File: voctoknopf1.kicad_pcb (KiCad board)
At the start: 2 copper layers, 161.2 x 88.5 mm, 47 parts, among them SW1 MX_D, SW10 MX_D, SW11 MX_D, SW12 MX_D, SW2 MX_D, SW3 MX_D, SW4 MX_D, SW5 MX_D, SW6 MX_D, SW7 MX_D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

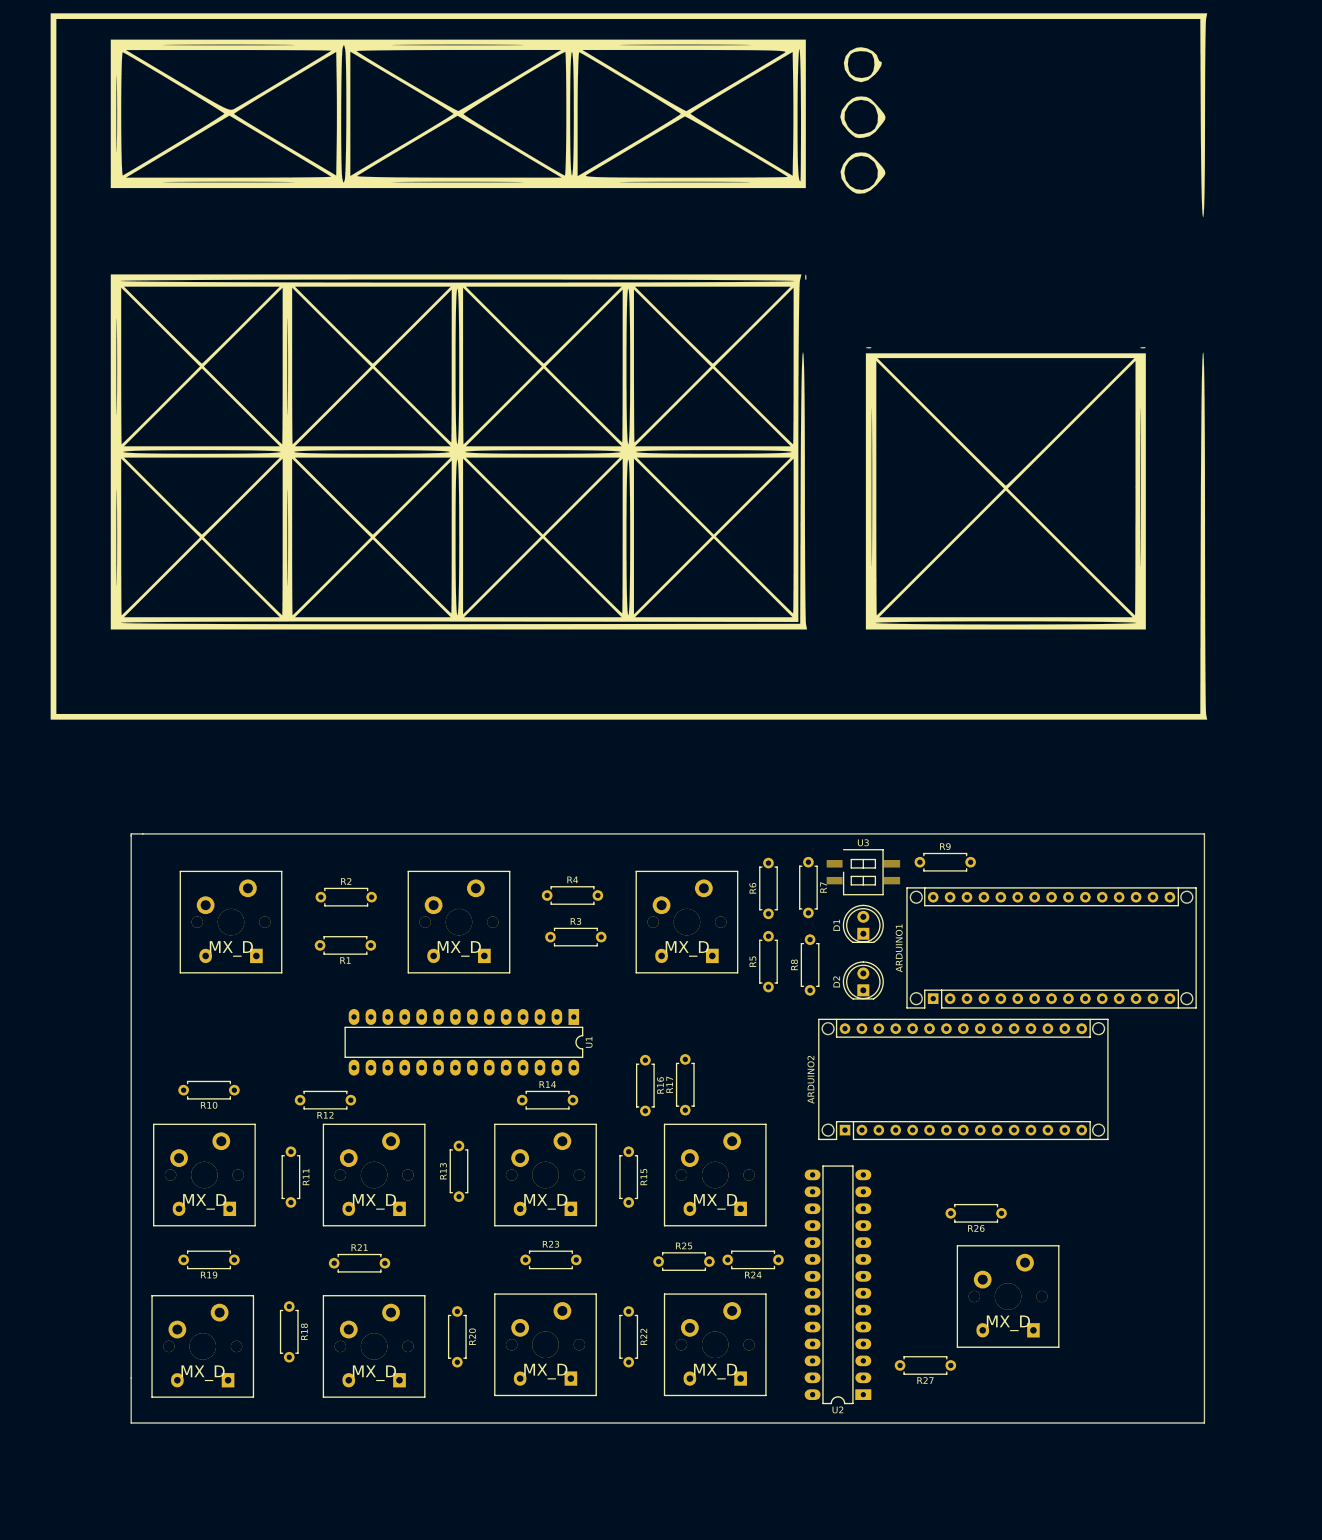
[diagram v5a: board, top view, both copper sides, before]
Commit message: ethernet shild the right way around
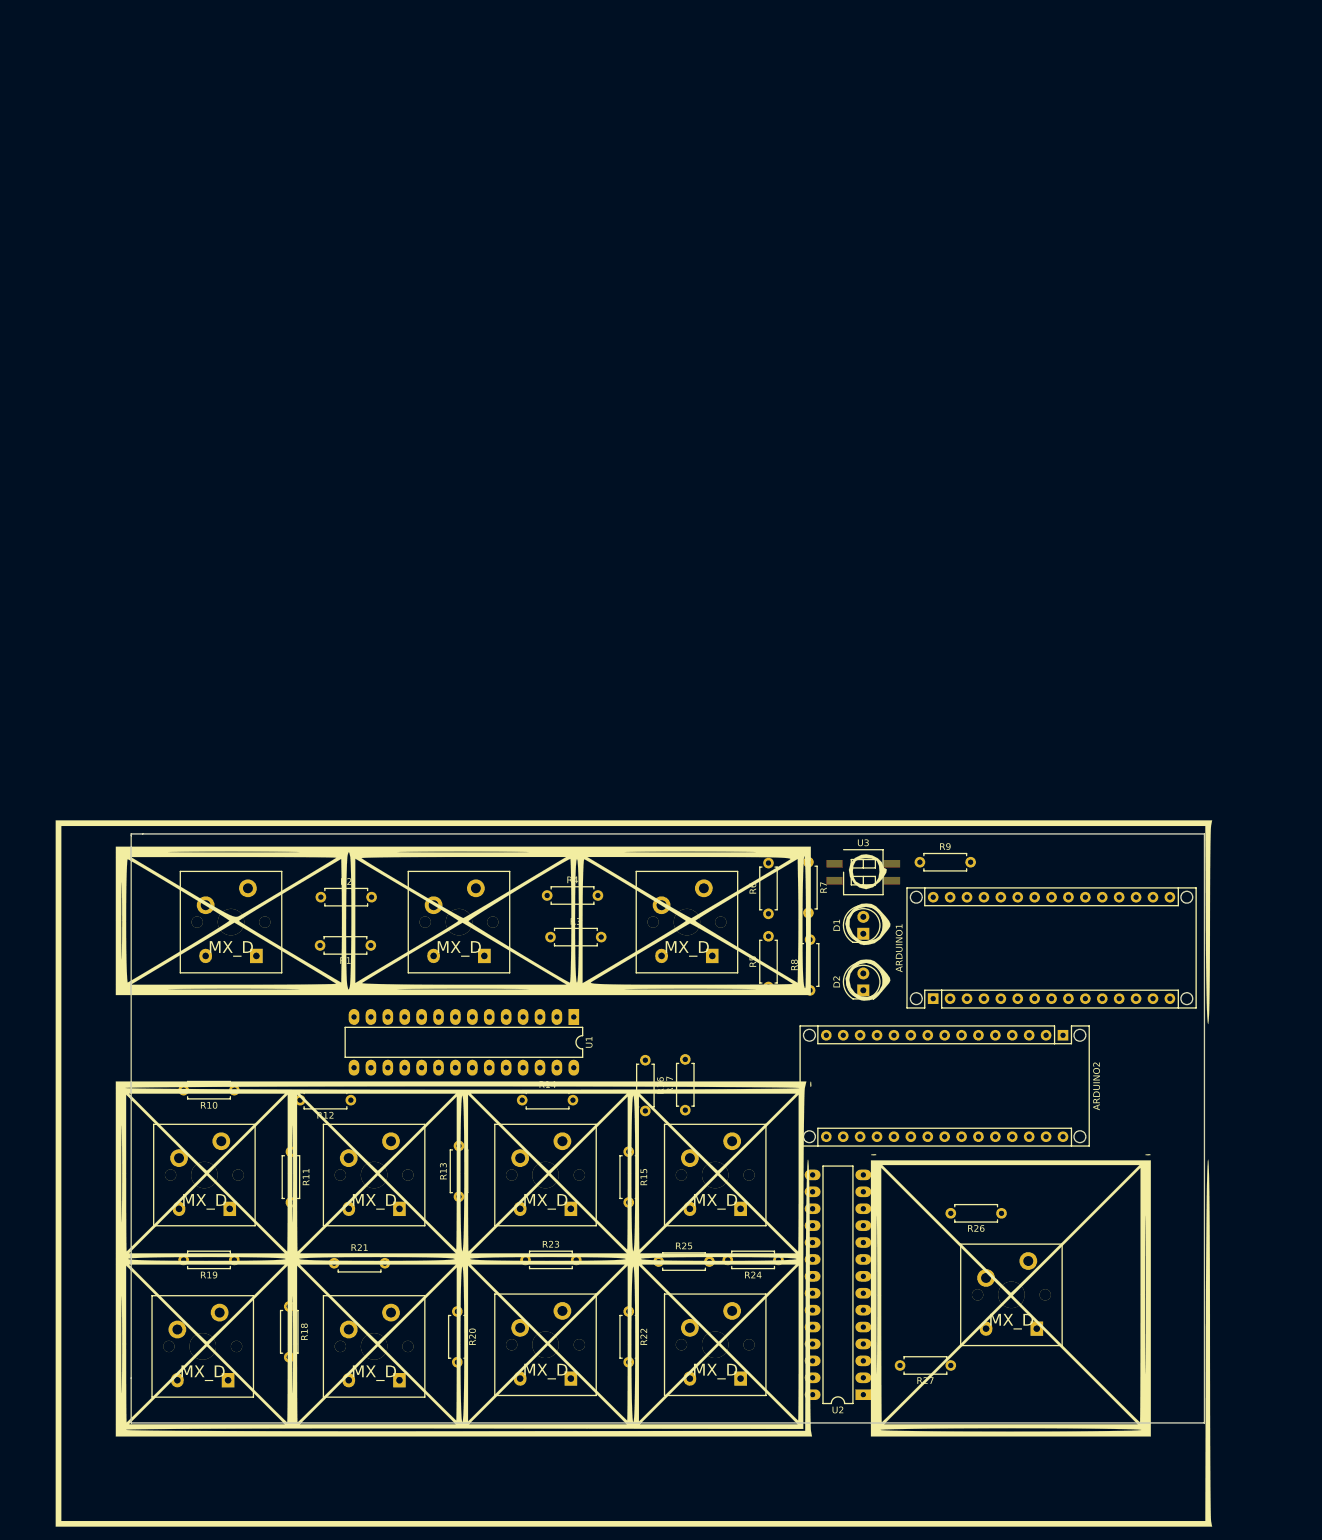
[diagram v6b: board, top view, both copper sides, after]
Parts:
- moved G*** 121.3 mm to (90.0, 66.5)
- moved ARDUINO2 35.7 mm to (156.2, 47.0), turned to 270 degrees
- moved SW12 0.56 mm to (148.5, 86.0)
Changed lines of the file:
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@@
     (links 118)
     (no_connects 118)
-    (area 16.174999 16.674999 177.575001 105.325001)
+    (area 4.654999 14.457221 179.185001 121.082778)
     (thickness 1.6)
     (drawings 7)
@@
   )
   (module cherry:SW_PCB_4PIN (layer F.Cu)
-    (at 148 86.25)
+    (at 148.5 86)
     (fp_text reference SW12 (at -4.445 -5.715) (layer F.SilkS) hide
       (effects (font (size 1.778 1.778) (thickness 0.2032)))
@@
   )
   (module Modules:Arduino_Nano_WithMountingHoles (layer F.Cu)
-    (at 123.5 61.25 90)
+    (at 156.25 47 270)
     (descr "Arduino Nano, http://www.mouser.com/pdfdocs/Gravitech_Arduino_Nano3_0.pdf")
     (tags "Arduino Nano")
-    (fp_text reference ARDUINO2 (at 7.62 -5.08 90) (layer F.SilkS)
-      (effects (font (size 1 1) (thickness 0.15)))
-    )
-    (fp_text value "Nano Ethernet Shield" (at 8.89 15.24 180) (layer F.Fab)
-      (effects (font (size 1 1) (thickness 0.15)))
-    )
-    (fp_text user %R (at 6.35 16.51 180) (layer F.Fab)
+    (fp_text reference ARDUINO2 (at 7.62 -5.08 270) (layer F.SilkS)
+      (effects (font (size 1 1) (thickness 0.15)))
+    )
+    (fp_text value "Nano Ethernet Shield" (at 8.89 15.24 360) (layer F.Fab)
+      (effects (font (size 1 1) (thickness 0.15)))
+    )
+    (fp_text user %R (at 6.35 16.51 360) (layer F.Fab)
       (effects (font (size 1 1) (thickness 0.15)))
     )
@@
     (fp_line (start 16.75 42.16) (end 16.75 -4.06) (layer F.CrtYd) (width 0.05))
     (fp_line (start 16.75 42.16) (end -1.53 42.16) (layer F.CrtYd) (width 0.05))
-    (pad 1 thru_hole rect (at 0 0 90) (size 1.6 1.6) (drill 0.8) (layers *.Cu *.Mask)
+    (pad 1 thru_hole rect (at 0 0 270) (size 1.6 1.6) (drill 0.8) (layers *.Cu *.Mask)
       (net 81 "Net-(ARDUINO2-Pad1)"))
-    (pad 17 thru_hole oval (at 15.24 33.02 90) (size 1.6 1.6) (drill 0.8) (layers *.Cu *.Mask)
+    (pad 17 thru_hole oval (at 15.24 33.02 270) (size 1.6 1.6) (drill 0.8) (layers *.Cu *.Mask)
       (net 59 "Net-(ARDUINO1-Pad17)"))
-    (pad 2 thru_hole oval (at 0 2.54 90) (size 1.6 1.6) (drill 0.8) (layers *.Cu *.Mask)
+    (pad 2 thru_hole oval (at 0 2.54 270) (size 1.6 1.6) (drill 0.8) (layers *.Cu *.Mask)
       (net 82 "Net-(ARDUINO2-Pad2)"))
-    (pad 18 thru_hole oval (at 15.24 30.48 90) (size 1.6 1.6) (drill 0.8) (layers *.Cu *.Mask)
+    (pad 18 thru_hole oval (at 15.24 30.48 270) (size 1.6 1.6) (drill 0.8) (layers *.Cu *.Mask)
       (net 83 "Net-(ARDUINO2-Pad18)"))
-    (pad 3 thru_hole oval (at 0 5.08 90) (size 1.6 1.6) (drill 0.8) (layers *.Cu *.Mask)
+    (pad 3 thru_hole oval (at 0 5.08 270) (size 1.6 1.6) (drill 0.8) (layers *.Cu *.Mask)
       (net 84 "Net-(ARDUINO2-Pad3)"))
-    (pad 19 thru_hole oval (at 15.24 27.94 90) (size 1.6 1.6) (drill 0.8) (layers *.Cu *.Mask)
+    (pad 19 thru_hole oval (at 15.24 27.94 270) (size 1.6 1.6) (drill 0.8) (layers *.Cu *.Mask)
       (net 85 "Net-(ARDUINO2-Pad19)"))
-    (pad 4 thru_hole oval (at 0 7.62 90) (size 1.6 1.6) (drill 0.8) (layers *.Cu *.Mask)
+    (pad 4 thru_hole oval (at 0 7.62 270) (size 1.6 1.6) (drill 0.8) (layers *.Cu *.Mask)
       (net 86 "Net-(ARDUINO2-Pad4)"))
-    (pad 20 thru_hole oval (at 15.24 25.4 90) (size 1.6 1.6) (drill 0.8) (layers *.Cu *.Mask)
+    (pad 20 thru_hole oval (at 15.24 25.4 270) (size 1.6 1.6) (drill 0.8) (layers *.Cu *.Mask)
       (net 87 "Net-(ARDUINO2-Pad20)"))
-    (pad 5 thru_hole oval (at 0 10.16 90) (size 1.6 1.6) (drill 0.8) (layers *.Cu *.Mask)
+    (pad 5 thru_hole oval (at 0 10.16 270) (size 1.6 1.6) (drill 0.8) (layers *.Cu *.Mask)
       (net 88 "Net-(ARDUINO2-Pad5)"))
-    (pad 21 thru_hole oval (at 15.24 22.86 90) (size 1.6 1.6) (drill 0.8) (layers *.Cu *.Mask)
+    (pad 21 thru_hole oval (at 15.24 22.86 270) (size 1.6 1.6) (drill 0.8) (layers *.Cu *.Mask)
       (net 89 "Net-(ARDUINO2-Pad21)"))
-    (pad 6 thru_hole oval (at 0 12.7 90) (size 1.6 1.6) (drill 0.8) (layers *.Cu *.Mask)
+    (pad 6 thru_hole oval (at 0 12.7 270) (size 1.6 1.6) (drill 0.8) (layers *.Cu *.Mask)
       (net 90 "Net-(ARDUINO2-Pad6)"))
-    (pad 22 thru_hole oval (at 15.24 20.32 90) (size 1.6 1.6) (drill 0.8) (layers *.Cu *.Mask)
+    (pad 22 thru_hole oval (at 15.24 20.32 270) (size 1.6 1.6) (drill 0.8) (layers *.Cu *.Mask)
       (net 91 "Net-(ARDUINO2-Pad22)"))
-    (pad 7 thru_hole oval (at 0 15.24 90) (size 1.6 1.6) (drill 0.8) (layers *.Cu *.Mask)
+    (pad 7 thru_hole oval (at 0 15.24 270) (size 1.6 1.6) (drill 0.8) (layers *.Cu *.Mask)
       (net 92 "Net-(ARDUINO2-Pad7)"))
-    (pad 23 thru_hole oval (at 15.24 17.78 90) (size 1.6 1.6) (drill 0.8) (layers *.Cu *.Mask)
+    (pad 23 thru_hole oval (at 15.24 17.78 270) (size 1.6 1.6) (drill 0.8) (layers *.Cu *.Mask)
       (net 93 "Net-(ARDUINO2-Pad23)"))
-    (pad 8 thru_hole oval (at 0 17.78 90) (size 1.6 1.6) (drill 0.8) (layers *.Cu *.Mask)
+    (pad 8 thru_hole oval (at 0 17.78 270) (size 1.6 1.6) (drill 0.8) (layers *.Cu *.Mask)
       (net 94 "Net-(ARDUINO2-Pad8)"))
-    (pad 24 thru_hole oval (at 15.24 15.24 90) (size 1.6 1.6) (drill 0.8) (layers *.Cu *.Mask)
+    (pad 24 thru_hole oval (at 15.24 15.24 270) (size 1.6 1.6) (drill 0.8) (layers *.Cu *.Mask)
       (net 95 "Net-(ARDUINO2-Pad24)"))
-    (pad 9 thru_hole oval (at 0 20.32 90) (size 1.6 1.6) (drill 0.8) (layers *.Cu *.Mask)
+    (pad 9 thru_hole oval (at 0 20.32 270) (size 1.6 1.6) (drill 0.8) (layers *.Cu *.Mask)
       (net 96 "Net-(ARDUINO2-Pad9)"))
-    (pad 25 thru_hole oval (at 15.24 12.7 90) (size 1.6 1.6) (drill 0.8) (layers *.Cu *.Mask)
+    (pad 25 thru_hole oval (at 15.24 12.7 270) (size 1.6 1.6) (drill 0.8) (layers *.Cu *.Mask)
       (net 97 "Net-(ARDUINO2-Pad25)"))
-    (pad 10 thru_hole oval (at 0 22.86 90) (size 1.6 1.6) (drill 0.8) (layers *.Cu *.Mask)
+    (pad 10 thru_hole oval (at 0 22.86 270) (size 1.6 1.6) (drill 0.8) (layers *.Cu *.Mask)
       (net 98 "Net-(ARDUINO2-Pad10)"))
-    (pad 26 thru_hole oval (at 15.24 10.16 90) (size 1.6 1.6) (drill 0.8) (layers *.Cu *.Mask)
+    (pad 26 thru_hole oval (at 15.24 10.16 270) (size 1.6 1.6) (drill 0.8) (layers *.Cu *.Mask)
       (net 99 "Net-(ARDUINO2-Pad26)"))
-    (pad 11 thru_hole oval (at 0 25.4 90) (size 1.6 1.6) (drill 0.8) (layers *.Cu *.Mask)
+    (pad 11 thru_hole oval (at 0 25.4 270) (size 1.6 1.6) (drill 0.8) (layers *.Cu *.Mask)
       (net 100 "Net-(ARDUINO2-Pad11)"))
-    (pad 27 thru_hole oval (at 15.24 7.62 90) (size 1.6 1.6) (drill 0.8) (layers *.Cu *.Mask)
+    (pad 27 thru_hole oval (at 15.24 7.62 270) (size 1.6 1.6) (drill 0.8) (layers *.Cu *.Mask)
       (net 101 "Net-(ARDUINO2-Pad27)"))
-    (pad 12 thru_hole oval (at 0 27.94 90) (size 1.6 1.6) (drill 0.8) (layers *.Cu *.Mask)
+    (pad 12 thru_hole oval (at 0 27.94 270) (size 1.6 1.6) (drill 0.8) (layers *.Cu *.Mask)
       (net 102 "Net-(ARDUINO2-Pad12)"))
-    (pad 28 thru_hole oval (at 15.24 5.08 90) (size 1.6 1.6) (drill 0.8) (layers *.Cu *.Mask)
+    (pad 28 thru_hole oval (at 15.24 5.08 270) (size 1.6 1.6) (drill 0.8) (layers *.Cu *.Mask)
       (net 103 "Net-(ARDUINO2-Pad28)"))
-    (pad 13 thru_hole oval (at 0 30.48 90) (size 1.6 1.6) (drill 0.8) (layers *.Cu *.Mask)
+    (pad 13 thru_hole oval (at 0 30.48 270) (size 1.6 1.6) (drill 0.8) (layers *.Cu *.Mask)
       (net 76 "Net-(ARDUINO1-Pad13)"))
-    (pad 29 thru_hole oval (at 15.24 2.54 90) (size 1.6 1.6) (drill 0.8) (layers *.Cu *.Mask)
-      (net 1 /GND))
-    (pad 14 thru_hole oval (at 0 33.02 90) (size 1.6 1.6) (drill 0.8) (layers *.Cu *.Mask)
+    (pad 29 thru_hole oval (at 15.24 2.54 270) (size 1.6 1.6) (drill 0.8) (layers *.Cu *.Mask)
+      (net 1 /GND))
+    (pad 14 thru_hole oval (at 0 33.02 270) (size 1.6 1.6) (drill 0.8) (layers *.Cu *.Mask)
       (net 77 "Net-(ARDUINO1-Pad14)"))
-    (pad 30 thru_hole oval (at 15.24 0 90) (size 1.6 1.6) (drill 0.8) (layers *.Cu *.Mask)
+    (pad 30 thru_hole oval (at 15.24 0 270) (size 1.6 1.6) (drill 0.8) (layers *.Cu *.Mask)
       (net 104 "Net-(ARDUINO2-Pad30)"))
-    (pad 15 thru_hole oval (at 0 35.56 90) (size 1.6 1.6) (drill 0.8) (layers *.Cu *.Mask)
+    (pad 15 thru_hole oval (at 0 35.56 270) (size 1.6 1.6) (drill 0.8) (layers *.Cu *.Mask)
       (net 79 "Net-(ARDUINO1-Pad15)"))
-    (pad 16 thru_hole oval (at 15.24 35.56 90) (size 1.6 1.6) (drill 0.8) (layers *.Cu *.Mask)
+    (pad 16 thru_hole oval (at 15.24 35.56 270) (size 1.6 1.6) (drill 0.8) (layers *.Cu *.Mask)
       (net 80 "Net-(ARDUINO1-Pad16)"))
-    (pad "" np_thru_hole circle (at 0 -2.54 90) (size 1.78 1.78) (drill 1.78) (layers *.Cu *.Mask))
-    (pad "" np_thru_hole circle (at 15.24 -2.54 90) (size 1.78 1.78) (drill 1.78) (layers *.Cu *.Mask))
-    (pad "" np_thru_hole circle (at 15.24 38.1 90) (size 1.78 1.78) (drill 1.78) (layers *.Cu *.Mask))
-    (pad "" np_thru_hole circle (at 0 38.1 90) (size 1.78 1.78) (drill 1.78) (layers *.Cu *.Mask))
+    (pad "" np_thru_hole circle (at 0 -2.54 270) (size 1.78 1.78) (drill 1.78) (layers *.Cu *.Mask))
+    (pad "" np_thru_hole circle (at 15.24 -2.54 270) (size 1.78 1.78) (drill 1.78) (layers *.Cu *.Mask))
+    (pad "" np_thru_hole circle (at 15.24 38.1 270) (size 1.78 1.78) (drill 1.78) (layers *.Cu *.Mask))
+    (pad "" np_thru_hole circle (at 0 38.1 270) (size 1.78 1.78) (drill 1.78) (layers *.Cu *.Mask))
   )
   (module library:Untitled10 (layer F.Cu)
-    (at 89.25 -54.75)
+    (at 90 66.5)
     (fp_text reference G*** (at 0 0) (layer F.SilkS) hide
       (effects (font (thickness 0.3)))

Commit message: pbc work
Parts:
- moved G*** 109.5 mm to (104.5, -42.0)
- moved SW12 0.56 mm to (148.0, 86.2)
- moved SW9 0.35 mm to (52.5, 93.5)
- moved SW4 0.25 mm to (27.0, 68.0)
- moved SW5 0.25 mm to (52.5, 68.0)
- moved SW8 0.25 mm to (27.0, 93.5)
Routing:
- net /GND: track 0.00 -> 547.4 mm
- net /5V: track 0.00 -> 370.0 mm
- net Net-(R2-Pad2): track 0.00 -> 91.7 mm
- net Net-(ARDUINO1-Pad16): track 0.00 -> 90.7 mm
- net Net-(ARDUINO1-Pad17): track 0.00 -> 84.0 mm
- net Net-(R11-Pad2): track 0.00 -> 71.5 mm, vias 0 -> 2
- net Net-(ARDUINO1-Pad10): track 0.00 -> 63.6 mm
- net Net-(ARDUINO1-Pad15): track 0.00 -> 56.6 mm
- net Net-(R6-Pad2): track 0.00 -> 53.2 mm
- net Net-(ARDUINO1-Pad14): track 0.00 -> 50.8 mm
- net Net-(R4-Pad2): track 0.00 -> 50.6 mm
- net Net-(ARDUINO1-Pad8): track 0.00 -> 49.5 mm
- net Net-(R5-Pad1): track 0.00 -> 46.9 mm
- net Net-(ARDUINO1-Pad13): track 0.00 -> 45.0 mm
- net Net-(R1-Pad1): track 0.00 -> 42.6 mm, vias 0 -> 1
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
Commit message: pcb
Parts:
- moved ARDUINO2 4.19 mm to (152.2, 45.8)
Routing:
- net Net-(ARDUINO1-Pad24): track 0.00 -> 149.4 mm, vias 0 -> 3
- net Net-(ARDUINO1-Pad23): track 0.00 -> 147.4 mm, vias 0 -> 3
- net Net-(R19-Pad2): track 10.6 -> 131.8 mm
- net Net-(R18-Pad1): track 0.00 -> 103.2 mm
- net Net-(R21-Pad2): track 12.1 -> 100.9 mm
- net Net-(R20-Pad1): track 0.00 -> 79.2 mm
- net Net-(R23-Pad2): track 13.7 -> 74.9 mm
- net /5V: track 370.0 -> 420.8 mm, vias 0 -> 1
- net Net-(R17-Pad2): track 0.00 -> 42.1 mm, vias 0 -> 1
- net Net-(R15-Pad2): track 0.00 -> 37.1 mm
- net Net-(R25-Pad2): track 11.2 -> 36.3 mm, vias 0 -> 1
- net Net-(R14-Pad2): track 0.00 -> 23.6 mm
- net Net-(R16-Pad1): track 0.00 -> 17.9 mm
- net Net-(R16-Pad2): track 0.00 -> 17.5 mm, vias 0 -> 2
- net Net-(R24-Pad1): track 0.00 -> 13.8 mm
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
